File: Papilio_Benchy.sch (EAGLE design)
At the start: 135 parts, among them IC1 FT2232H, IC2 93C46, J1 USB MICRO, J4 HDMI-TYPE-A-RECEPTICALFCI1002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, SW1 SWITCH-2CH-6P-3010010P1, SW2 EVQQ2, T1 MOSFET-NCHANNELSMD, U1 ATMEGA32U4-XUMU, U11 PCA9306, U2 LTC3419EMS, U5 ARDUINO_MEGA_SHIELD, X2 12MHz, Y1 16MHz KX-7

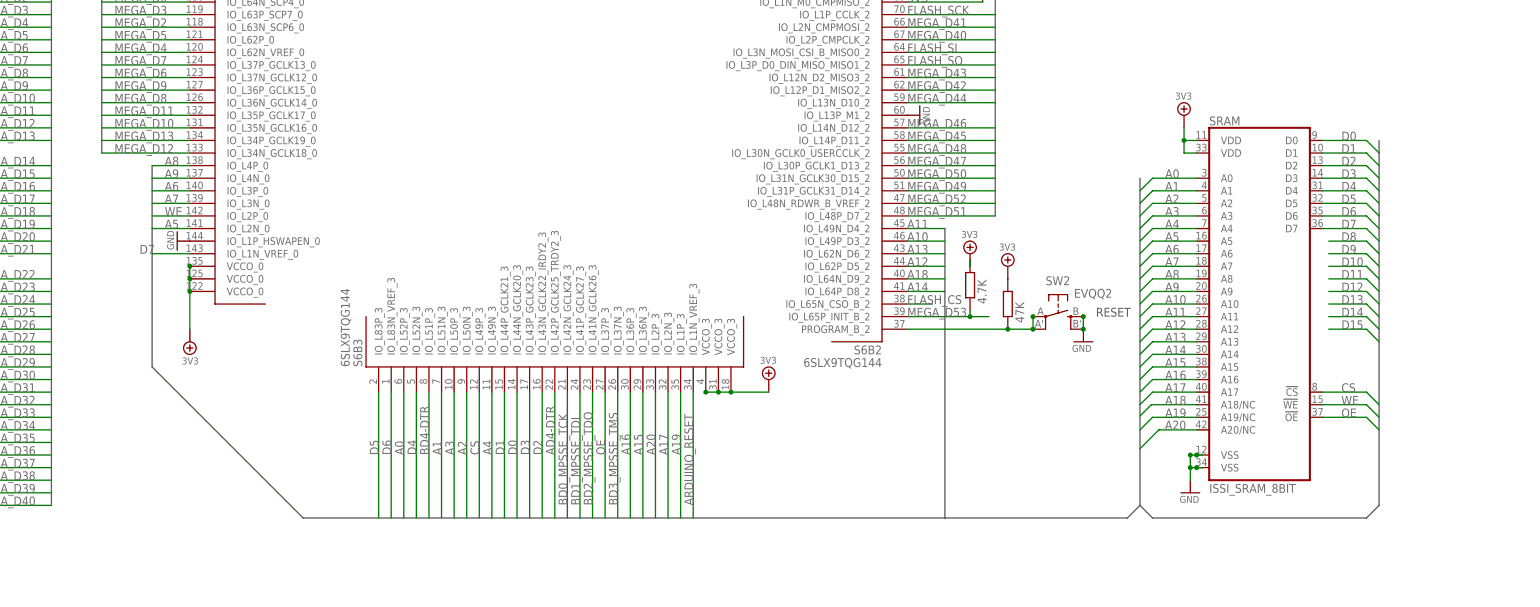
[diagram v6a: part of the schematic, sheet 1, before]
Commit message: Sram initiallly routed.
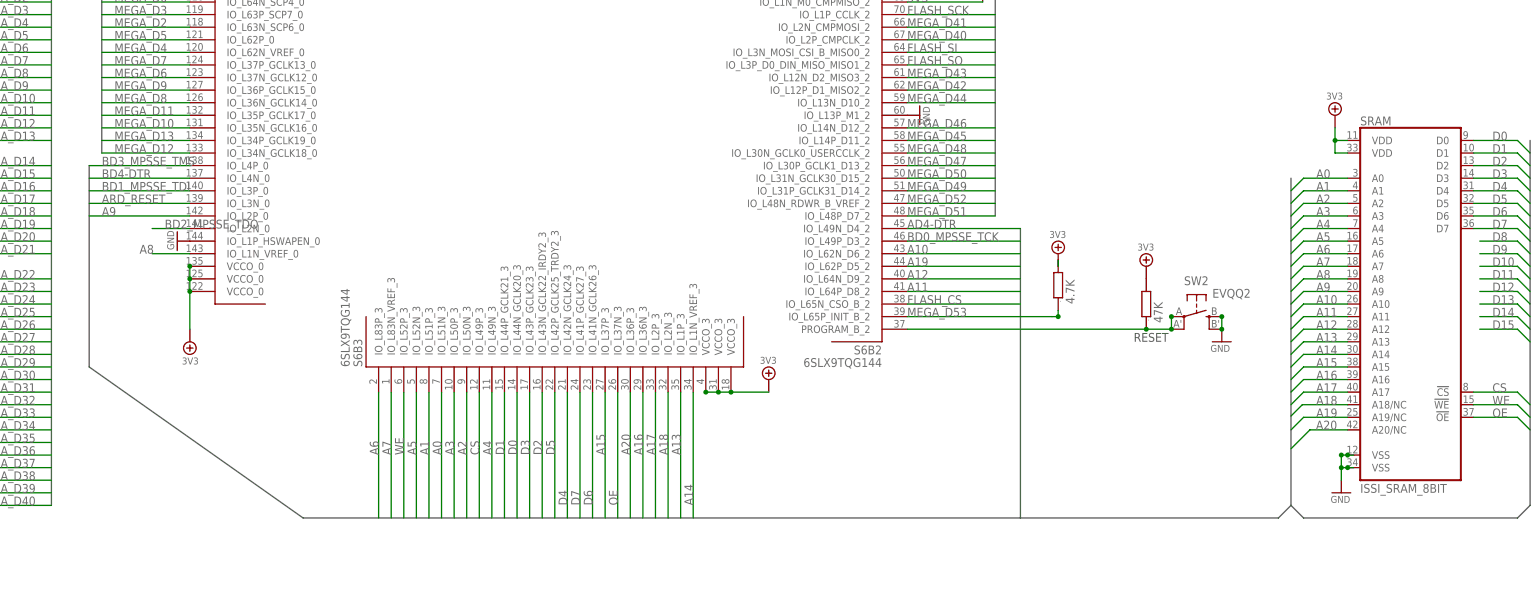
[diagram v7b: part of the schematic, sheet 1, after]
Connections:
- removed net ARDUINO_RESET: D2.A, R7A.1, S6B3.IO_L1N_VREF_3, U1.RESET
- new net ARD_RESET: D2.A, R7A.1, S6B0.IO_L3N_0, U1.RESET
- net A0: now also S6B3.IO_L51N_3; no longer S6B3.IO_L52P_3
- net A1: now also S6B3.IO_L51P_3; no longer S6B3.IO_L51N_3
- net A10: now also S6B2.IO_L62N_D6_2; no longer S6B2.IO_L49P_D3_2
- net A11: now also S6B2.IO_L64P_D8_2; no longer S6B2.IO_L49N_D4_2
- net A12: now also S6B2.IO_L64N_D9_2; no longer S6B2.IO_L62P_D5_2
- net A13: now also S6B3.IO_L1P_3; no longer S6B2.IO_L62N_D6_2
- net A14: now also S6B3.IO_L1N_VREF_3; no longer S6B2.IO_L64P_D8_2
- net A15: now also S6B3.IO_L37P_3; no longer S6B3.IO_L36N_3
- net A16: now also S6B3.IO_L36N_3; no longer S6B3.IO_L36P_3
- net A17: now also S6B3.IO_L2P_3; no longer S6B3.IO_L2N_3
- net A18: now also S6B3.IO_L2N_3; no longer S6B2.IO_L64N_D9_2
- net A19: now also S6B2.IO_L62P_D5_2; no longer S6B3.IO_L1P_3
- net A20: now also S6B3.IO_L36P_3; no longer S6B3.IO_L2P_3
- net A5: now also S6B3.IO_L52N_3; no longer S6B0.IO_L2N_0
- net A6: now also S6B3.IO_L83P_3; no longer S6B0.IO_L3P_0
- net A7: now also S6B3.IO_L83N_VREF_3; no longer S6B0.IO_L3N_0
- net A8: now also S6B0.IO_L1N_VREF_0; no longer S6B0.IO_L4P_0
- net A9: now also S6B0.IO_L2P_0; no longer S6B0.IO_L4N_0
- net AD4-DTR: now also S6B2.IO_L49N_D4_2; no longer S6B3.IO_L42P_GCLK25_TRDY2_3
- net BD0_MPSSE_TCK: now also S6B2.IO_L49P_D3_2; no longer S6B3.IO_L42N_GCLK24_3
- net BD1_MPSSE_TDI: now also S6B0.IO_L3P_0; no longer S6B3.IO_L41P_GCLK27_3
- net BD2_MPSSE_TDO: now also S6B0.IO_L2N_0; no longer S6B3.IO_L41N_GCLK26_3
- net BD3_MPSSE_TMS: now also S6B0.IO_L4P_0; no longer S6B3.IO_L37N_3
- net BD4-DTR: now also S6B0.IO_L4N_0; no longer S6B3.IO_L51P_3
- net D4: now also S6B3.IO_L42N_GCLK24_3; no longer S6B3.IO_L52N_3
- net D5: now also S6B3.IO_L42P_GCLK25_TRDY2_3; no longer S6B3.IO_L83P_3
- net D6: now also S6B3.IO_L41N_GCLK26_3; no longer S6B3.IO_L83N_VREF_3
- net D7: now also S6B3.IO_L41P_GCLK27_3; no longer S6B0.IO_L1N_VREF_0
- net OE: now also S6B3.IO_L37N_3; no longer S6B3.IO_L37P_3
- net WE: now also S6B3.IO_L52P_3; no longer S6B0.IO_L2P_0
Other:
- moved on the sheet: SRAM, SW2

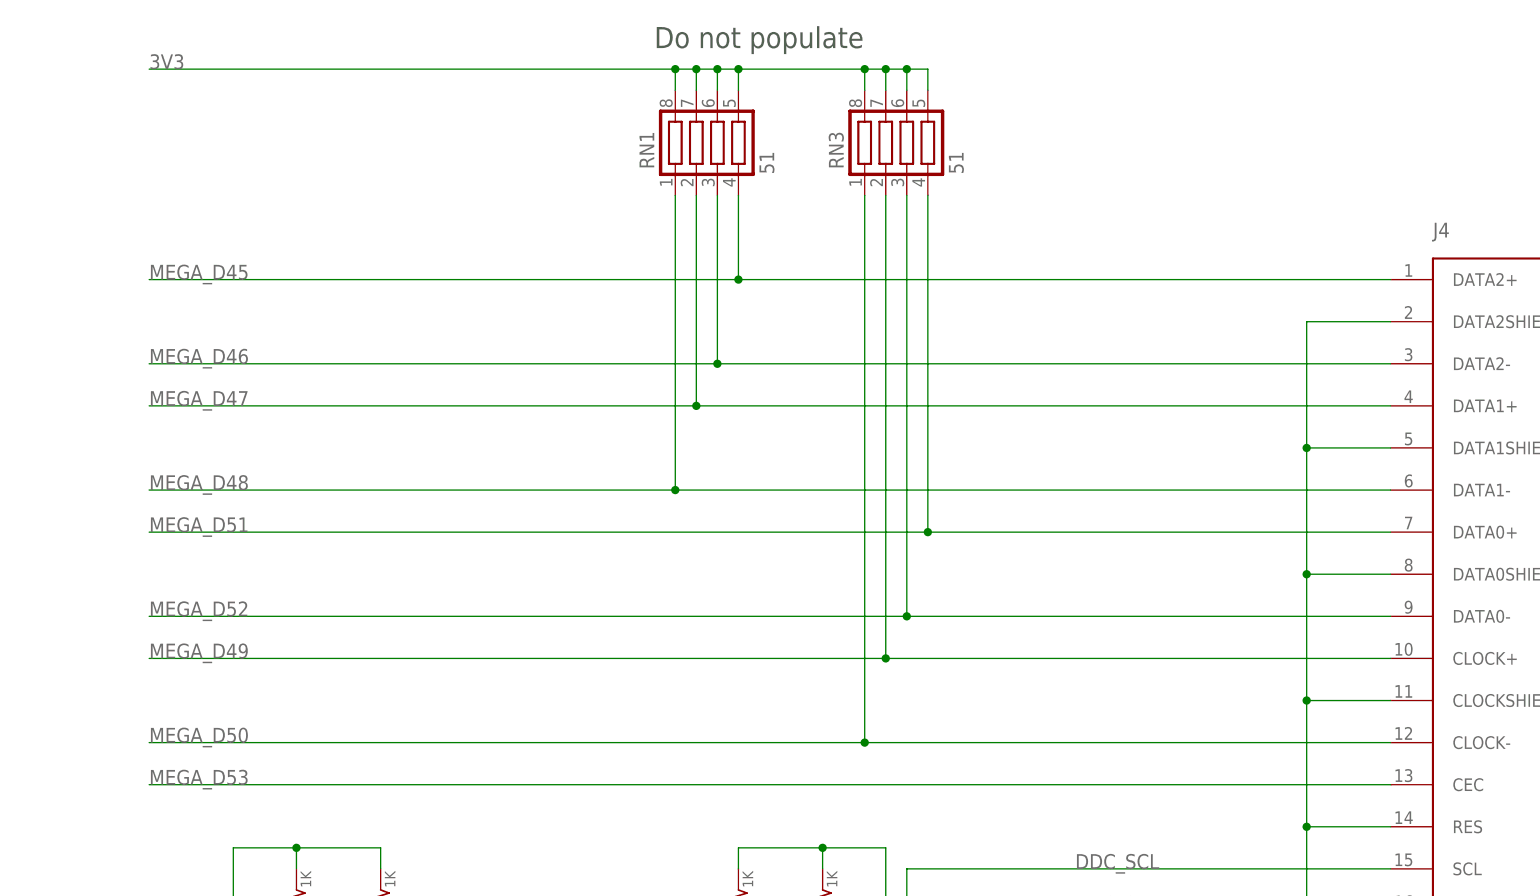
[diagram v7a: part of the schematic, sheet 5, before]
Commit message: Place and route FT2232H
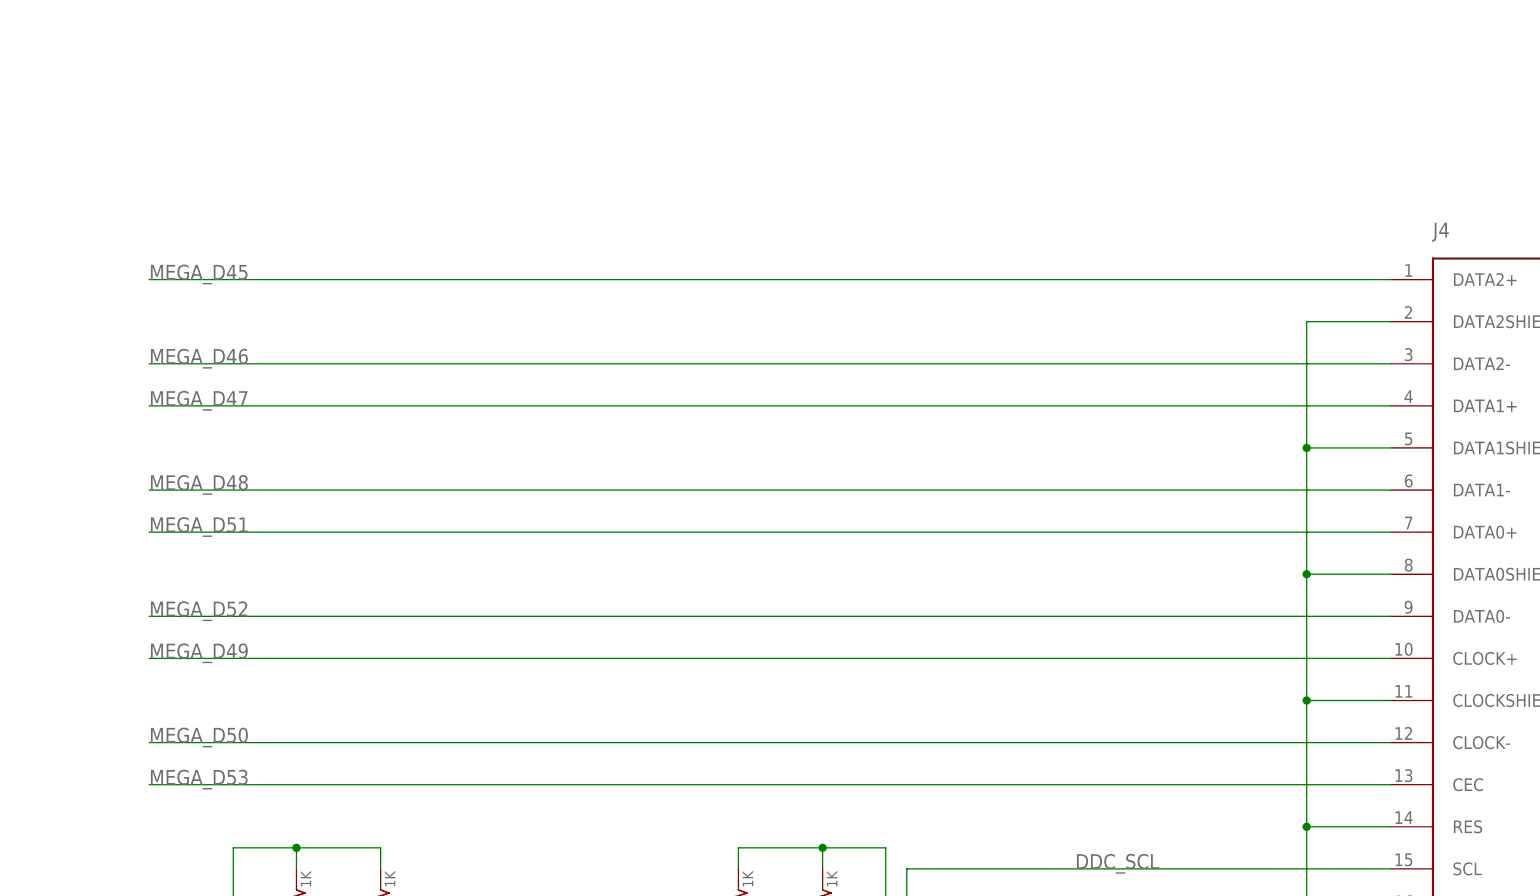
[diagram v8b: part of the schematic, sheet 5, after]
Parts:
- removed IC2: 93C46, dp_devices:93C46
- removed RN1, RN3: 51, saanlima:CTS742C083
- added U3: 93C46B, Bogdan_Commons:DIGITAL-EEPROM-MICROWIRE-6P_SOT23
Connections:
- net DM renamed FTUSB_N
- net DP renamed FTUSB_P
- removed net 3.3V: C2.1, C38.1, C39.1, C40.1, C41.1, IC1.VCCIO0, IC1.VCCIO1, IC1.VCCIO2, IC1.VCCIO3, IC1.VREGIN, IC2.ORG, IC2.VCC, L4.2, L5.2, R34.1, R36.2, R38.2, R39.2, RX1.A, TX1.A
- net 3V3: now also C2.1, C38.1, C39.1, C40.1, C41.1, IC1.VCCIO0, IC1.VCCIO1, IC1.VCCIO2, IC1.VCCIO3, IC1.VREGIN, L4.2, L5.2, R34.1, R36.2, R38.2, R39.2, RX1.A, TX1.A, U3.VCC; no longer RN1.5, RN1.6, RN1.7, RN1.8, RN3.5, RN3.6, RN3.7, RN3.8
- net ATMEGA_A0: now also U1.(ADC0)PF0; no longer U1.(ADC7/TDI)PF7
- net ATMEGA_A1: now also U1.(ADC1)PF1; no longer U1.(ADC6/TDO)PF6
- net ATMEGA_A2: now also U1.(ADC4/TCK)PF4; no longer U1.(ADC5/TMS)PF5
- net ATMEGA_A3: now also U1.(ADC5/TMS)PF5; no longer U1.(ADC4/TCK)PF4
- net ATMEGA_A4: now also U1.(ADC6/TDO)PF6; no longer U1.(ADC1)PF1
- net ATMEGA_A5: now also U1.(ADC7/TDI)PF7; no longer U1.(ADC0)PF0
- net ATMEGA_D4: now also U1.(OC3A/#0C4A)PC6; no longer U1.(ICP1/ADC8)PD4
- net ATMEGA_D5*: now also U1.(PCINT6/OC1B/OC4B/ADC13)PB6; no longer U1.(OC3A/#0C4A)PC6
- net ATMEGA_D6*: now also U1.(PCINT5/OC1A/#OC4B/ADC12)PB5; no longer U1.(T0/OC4D/ADC10)PD7
- net ATMEGA_D7: now also U1.(ADC11/PCINT4)PB4; no longer U1.(INT6/AIN0)PE6
- net ATMEGA_IO10*: now also U1.(ICP1/ADC8)PD4; no longer U1.(PCINT6/OC1B/OC4B/ADC13)PB6
- net ATMEGA_IO12: now also U1.(INT6/AIN0)PE6; no longer U1.(T1/#OC4D/ADC9)PD6
- net ATMEGA_IO8: now also U1.(T0/OC4D/ADC10)PD7; no longer U1.(ADC11/PCINT4)PB4
- net ATMEGA_IO9*: now also U1.(T1/#OC4D/ADC9)PD6; no longer U1.(PCINT5/OC1A/#OC4B/ADC12)PB5
- net BD1_MPSSE_TDI: now also S6B0.IO_L2N_0; no longer S6B0.IO_L3P_0
- net BD2_MPSSE_TDO: now also S6B0.IO_L3P_0; no longer S6B0.IO_L2N_0
- net EECLK: now also U3.CLK; no longer IC2.SK
- net EECS: now also U3.CS; no longer IC2.CS
- net EEDATA: now also U3.DI; no longer IC2.DI
- net GND: now also U3.GND; no longer IC2.GND
- net MEGA_D45: no longer RN1.4
- net MEGA_D46: no longer RN1.3
- net MEGA_D47: no longer RN1.2
- net MEGA_D48: no longer RN1.1
- net MEGA_D49: no longer RN3.2
- net MEGA_D50: no longer RN3.1
- net MEGA_D51: no longer RN3.4
- net MEGA_D52: no longer RN3.3
- net N$45: now also U3.DO; no longer IC2.DO
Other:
- note removed: "Do not populate"
